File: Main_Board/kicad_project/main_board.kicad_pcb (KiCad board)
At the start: 4 copper layers, 235 parts, among them J1 MOTOR, J10 USB_B_Micro, J11 DATA_UART, J12 I2C_EXTERNAL, J13 DEBUG_HEADER, J14 IO1, J15 IO7, J16 IO2, J17 IO3, J18 IO8, J19 IO9, J2 MOTOR, J20 IO4, J21 IO5, J22 IO10, J23 IO6, J24 EXPANSION_HEADER, J3 MOTOR, J4 MOTOR, J5 PWR_ENTRY, J6 12V_HDR, J7 3V3_HDR, J8 5V_HDR, J9 I2C_BUFFERED, SW1 SW_SPST, U1 TMC2209, U2 TMC2209, U3 TMC2209, U4 TMC2209, U5 TPS562200, U6 TPS562200, U7 PCA9600DP, U8 USBLC6-2SC6, U9 STM32G474VxT, Y1 ABS06-32.768kHz, Y2 DNP

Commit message: edits to stepper layout
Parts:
- moved TP2 116.9 mm to (102.3, 53.3)
- moved TP3 116.9 mm to (130.8, 53.3)
- moved TP4 115.7 mm to (158.9, 53.3)
- moved TP1 115.6 mm to (74.3, 53.3)
- moved C11 113.0 mm to (100.7, 42.4)
- moved C13 113.0 mm to (103.1, 43.9)
- moved C17 113.0 mm to (98.2, 34.9)
- moved C18 113.0 mm to (92.0, 32.9)
- moved C2 113.0 mm to (72.7, 42.4)
- moved C20 113.0 mm to (129.1, 42.4)
- moved C25 113.0 mm to (142.0, 34.9)
- moved C26 113.0 mm to (126.4, 34.9)
- moved C28 113.0 mm to (167.0, 41.6)
- moved C29 113.0 mm to (157.3, 42.4)
- moved C31 113.0 mm to (159.7, 43.9)
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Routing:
- added copper zone on In2.Cu, net +12V
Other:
- board outline added: 150 x 150 mm

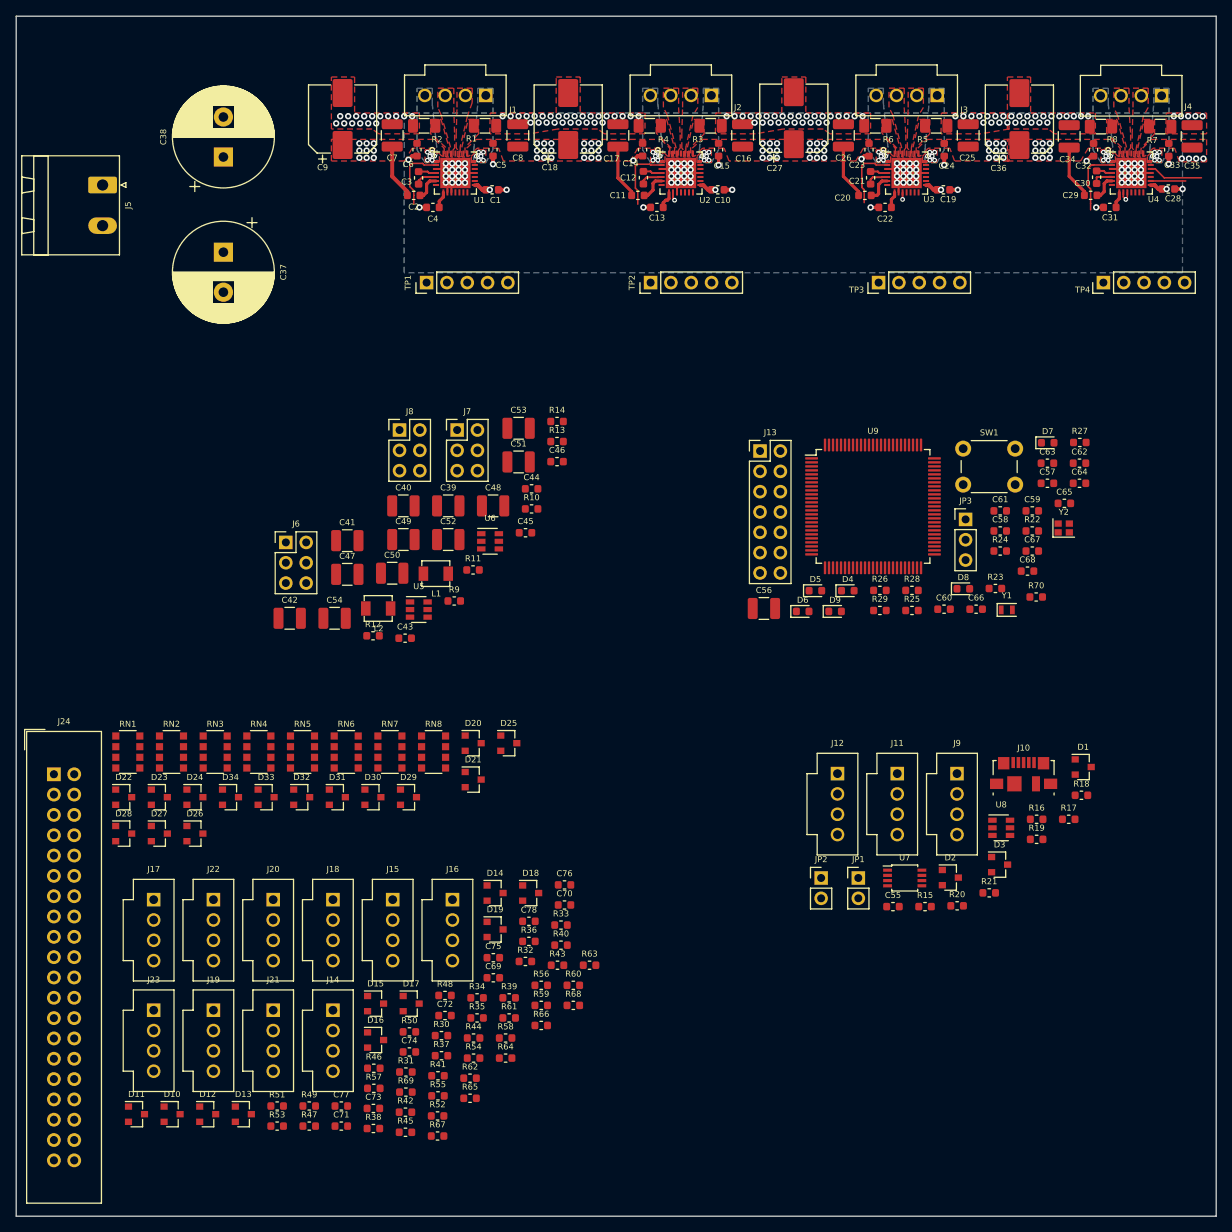
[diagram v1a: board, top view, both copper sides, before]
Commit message: regulators layout done
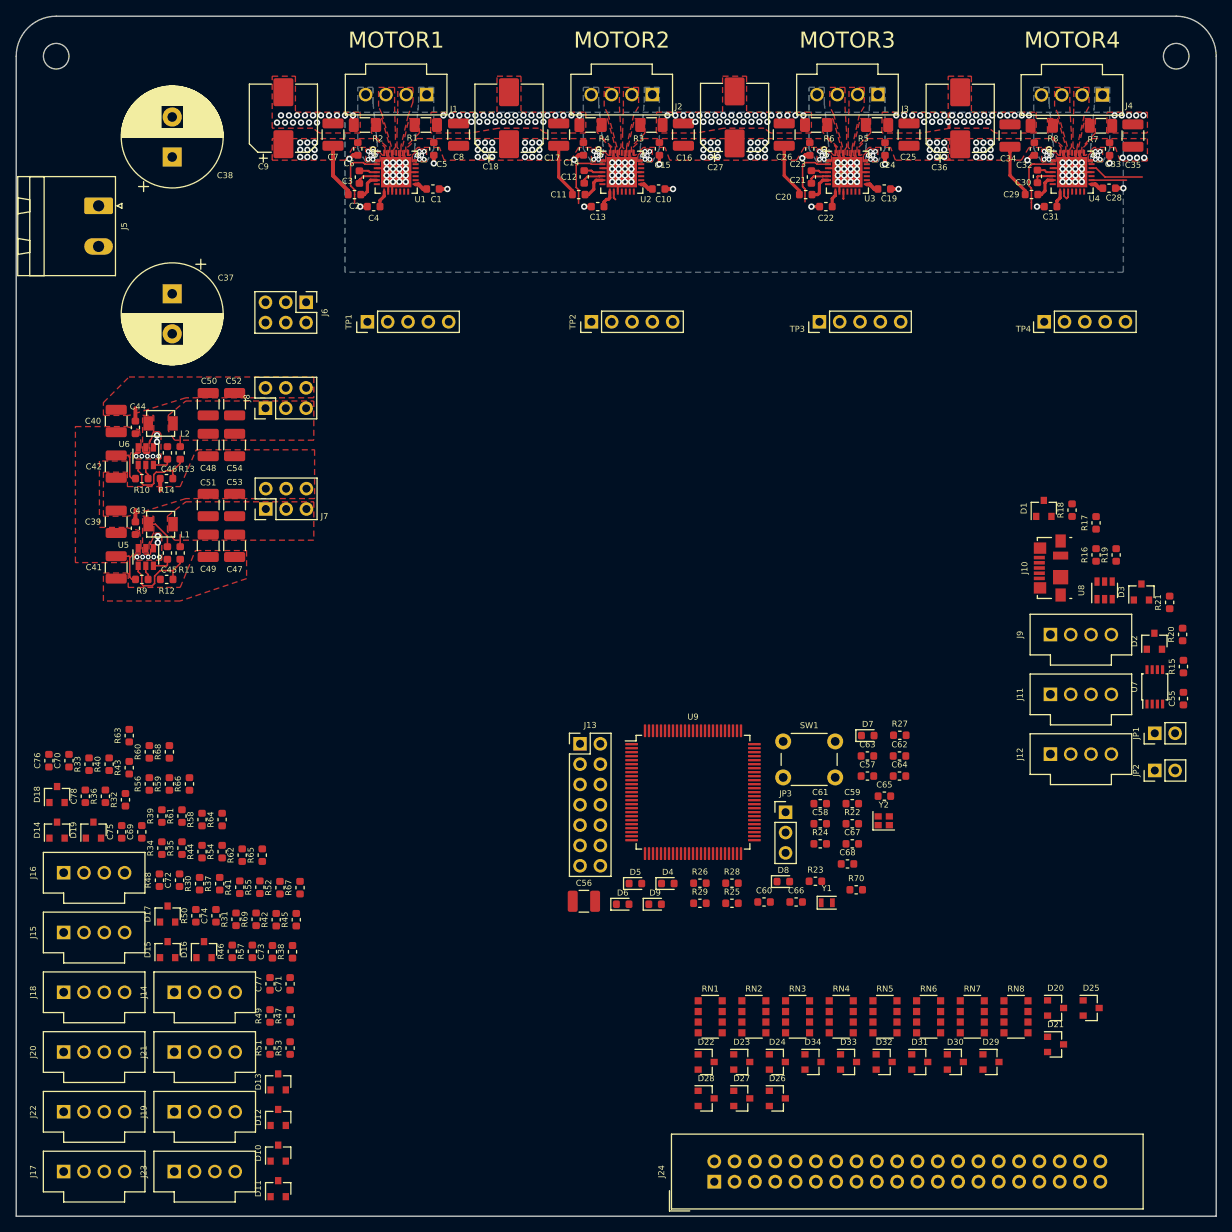
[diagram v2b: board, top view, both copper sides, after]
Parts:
- added REF**: MountingHole_3.2mm_M3, MountingHole:MountingHole_3.2mm_M3, F.Cu at (28.0, 25.0)
- added REF**: MountingHole_3.2mm_M3, MountingHole:MountingHole_3.2mm_M3, F.Cu at (168.0, 25.0)
- moved J24 97.0 mm to (110.3, 165.7), turned to 90 degrees
- moved RN1 80.0 mm to (109.8, 145.1)
- moved RN3 80.0 mm to (120.7, 145.1)
- moved RN5 80.0 mm to (131.6, 145.1)
- moved D23 80.0 mm to (113.7, 150.7)
- moved D24 80.0 mm to (118.1, 150.7)
- moved D25 80.0 mm to (157.4, 144.0)
- moved D26 80.0 mm to (118.1, 155.3)
- moved D27 80.0 mm to (113.7, 155.3)
- moved D29 80.0 mm to (144.8, 150.7)
- moved D31 80.0 mm to (135.9, 150.7)
- moved D32 80.0 mm to (131.5, 150.7)
- moved RN2 80.0 mm to (115.2, 145.1)
- moved RN4 80.0 mm to (126.1, 145.1)
- moved RN7 80.0 mm to (142.5, 145.1)
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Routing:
- net Net-(R13-Pad2): track 0.00 -> 11.5 mm
- net Net-(R11-Pad2): track 0.00 -> 10.7 mm
- net +12V: track 27.3 -> 37.5 mm
- net GND: track 45.7 -> 50.3 mm, vias 184 -> 198
- net Net-(C45-Pad1): track 0.00 -> 3.73 mm
- net Net-(C46-Pad2): track 0.00 -> 2.85 mm
- net Net-(C45-Pad2): track 0.00 -> 2.50 mm
- net Net-(R9-Pad1): track 0.00 -> 1.82 mm
- net Net-(R10-Pad1): track 0.00 -> 1.82 mm
- net +5V: track 0.00 -> 1.30 mm
- net +3V3: track 12.4 -> 11.9 mm, vias 7 -> 0
- added copper zone on F.Cu, net +3V3
- added copper zone on F.Cu, net +5V
- added copper zone on F.Cu, net Net-(C45-Pad1)
- added copper zone on F.Cu, net Net-(C46-Pad1)
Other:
- outline, holes or cut-outs redrawn
- board text added: "MOTOR1"
- board text added: "MOTOR2"
- board text added: "MOTOR3"
- board text added: "MOTOR4"

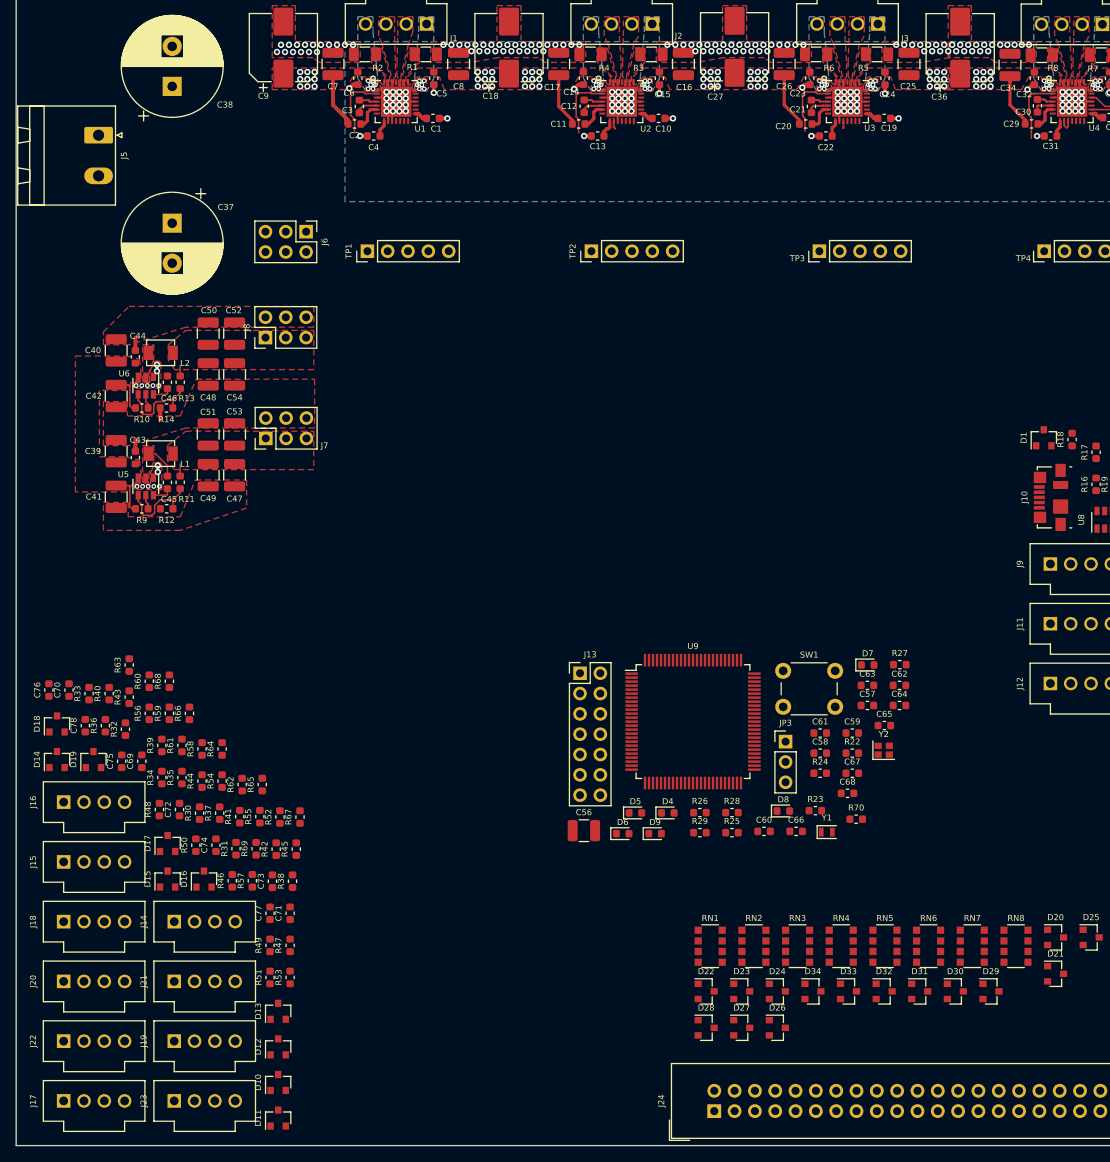
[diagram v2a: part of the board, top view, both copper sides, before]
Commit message: limit switch layout
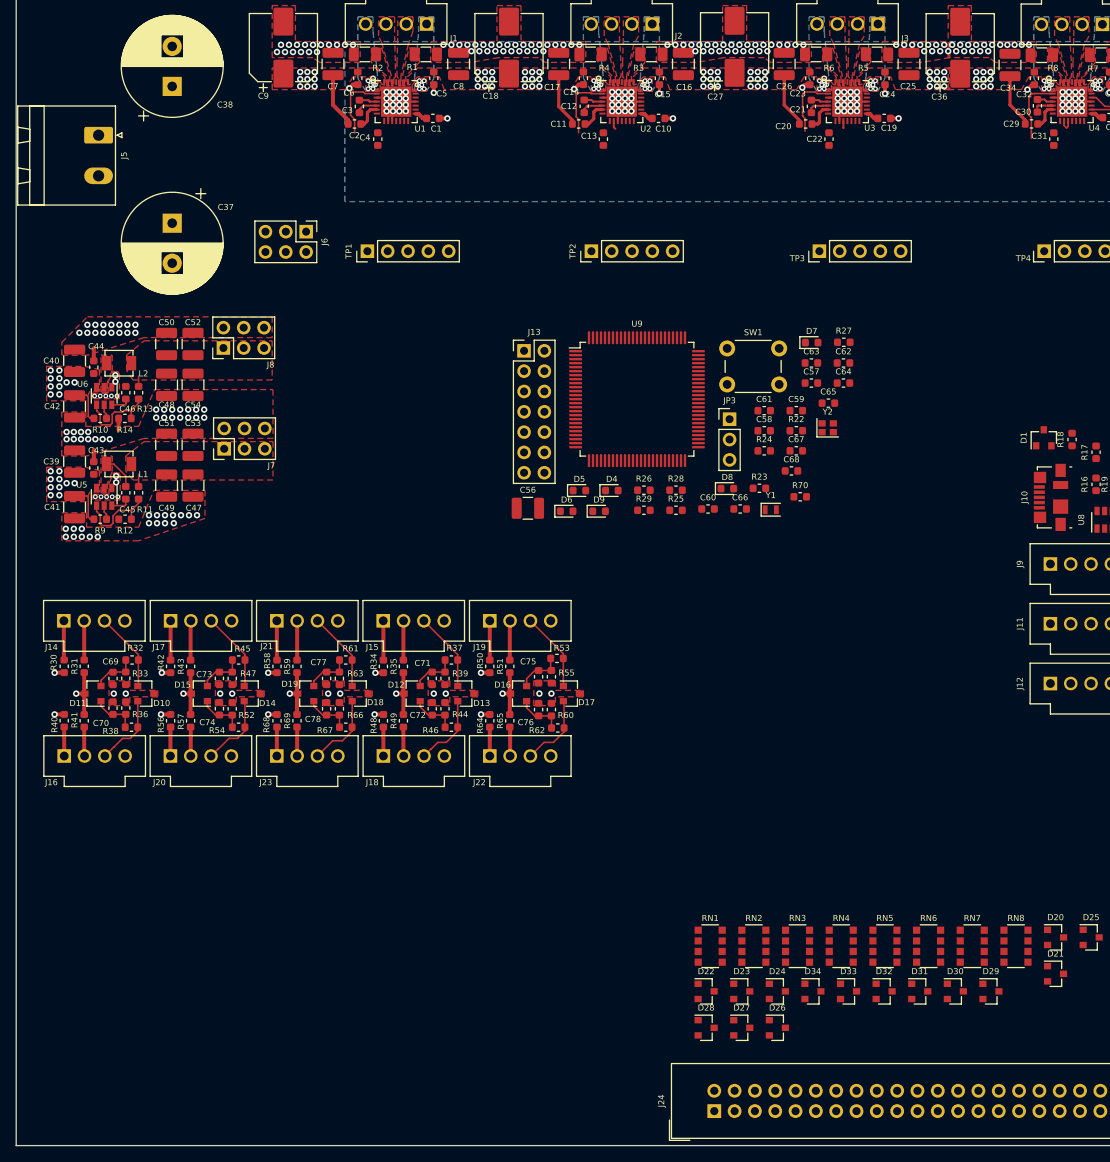
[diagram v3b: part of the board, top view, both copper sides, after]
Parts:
- moved J19 65.7 mm to (82.2, 104.4)
- moved J22 64.1 mm to (82.2, 121.3)
- moved J17 61.5 mm to (42.3, 104.4)
- moved C76 61.3 mm to (88.3, 115.5), turned to 270 degrees
- moved D11 57.9 mm to (32.6, 113.5), turned to 180 degrees
- moved D17 53.8 mm to (92.4, 113.5), turned to 0 degrees
- moved C75 53.2 mm to (88.3, 111.4), turned to 270 degrees
- moved R53 52.0 mm to (90.6, 109.1), turned to 0 degrees
- moved D10 51.3 mm to (39.2, 113.5), turned to 0 degrees
- moved R60 50.4 mm to (89.9, 115.5), turned to 270 degrees
- moved J15 50.0 mm to (68.9, 104.4)
- moved R51 49.1 mm to (84.7, 110.1)
- moved D12 47.2 mm to (72.5, 113.5), turned to 180 degrees
- moved J21 46.9 mm to (55.6, 104.4)
- moved D13 46.1 mm to (79.2, 113.5), turned to 0 degrees
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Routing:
- net +3V3: track 11.9 -> 43.5 mm, vias 0 -> 5
- net +12V: track 37.5 -> 48.7 mm, vias 67 -> 97
- net Net-(D18-Pad1): track 0.00 -> 9.95 mm
- net Net-(D14-Pad1): track 0.00 -> 9.94 mm
- net Net-(D10-Pad1): track 0.00 -> 9.94 mm
- net Net-(D13-Pad1): track 0.00 -> 9.91 mm
- net Net-(D17-Pad1): track 0.00 -> 9.86 mm
- net Net-(D18-Pad2): track 0.00 -> 9.35 mm
- net Net-(D17-Pad2): track 0.00 -> 9.32 mm
- net Net-(D14-Pad2): track 0.00 -> 9.28 mm
- net Net-(D13-Pad2): track 0.00 -> 9.23 mm
- net Net-(D10-Pad2): track 0.00 -> 9.14 mm
- net /Limit Switches/IO9: track 0.00 -> 5.99 mm
- net /Limit Switches/IO10: track 0.00 -> 5.85 mm
- net /Limit Switches/IO2: track 0.00 -> 5.80 mm
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
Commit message: expansion connector - rev 1.1 schematic, finished layout
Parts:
- moved D27 40.4 mm to (153.8, 151.2), turned to 90 degrees
- moved D20 40.3 mm to (113.3, 151.1), turned to 90 degrees
- moved D23 37.2 mm to (150.8, 147.7), turned to 90 degrees
- moved D22 30.1 mm to (139.2, 147.7), turned to 90 degrees
- moved D25 30.0 mm to (127.5, 147.6), turned to 90 degrees
- moved D21 28.2 mm to (124.8, 151.1), turned to 90 degrees
- moved D34 25.5 mm to (148.1, 151.2), turned to 90 degrees
- moved D26 24.5 mm to (142.2, 151.2), turned to 90 degrees
- moved D31 20.8 mm to (156.6, 147.7), turned to 90 degrees
- moved D29 14.2 mm to (130.7, 151.1), turned to 90 degrees
- moved J10 14.1 mm to (163.0, 79.8)
- moved RN8 13.8 mm to (155.5, 156.6), turned to 270 degrees
- moved RN7 13.6 mm to (149.7, 156.6), turned to 270 degrees
- moved RN6 13.4 mm to (143.9, 156.6), turned to 270 degrees
- moved RN5 13.2 mm to (138.1, 156.6), turned to 270 degrees
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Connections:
- D22 pad 1: /MCU/EXP_IO16 -> /MCU/EXP_IO17
- D22 pad 2: /MCU/EXP_IO17 -> /MCU/EXP_IO18
- D23 pad 1: /MCU/EXP_IO24 -> /MCU/EXP_IO25
- D23 pad 2: /MCU/EXP_IO25 -> /MCU/EXP_IO26
- D26 pad 1: /MCU/EXP_IO18 -> /MCU/EXP_IO19
- D26 pad 2: /MCU/EXP_IO19 -> /MCU/EXP_IO20
- D27 pad 1: /MCU/EXP_IO26 -> /MCU/EXP_IO27
- D27 pad 2: /MCU/EXP_IO27 -> /MCU/EXP_IO28
- D30 pad 1: /MCU/EXP_IO20 -> /MCU/EXP_IO21
- D30 pad 2: /MCU/EXP_IO21 -> /MCU/EXP_IO22
- D31 pad 1: /MCU/EXP_IO28 -> /MCU/EXP_IO29
- D31 pad 2: /MCU/EXP_IO29 -> /MCU/EXP_IO30
- D33 pad 2: /MCU/EXP_IO30 -> /MCU/EXP_IO16
- D34 pad 1: /MCU/EXP_IO22 -> /MCU/EXP_IO23
- D34 pad 2: /MCU/EXP_IO23 -> /MCU/EXP_IO24
- RN1 pad 1: /MCU/EXP_IO1 -> /MCU/EXP_IO4
- RN1 pad 2: /MCU/EXP_IO2 -> /MCU/EXP_IO3
- RN1 pad 3: /MCU/EXP_IO3 -> /MCU/EXP_IO2
- RN1 pad 4: /MCU/EXP_IO4 -> /MCU/EXP_IO1
- RN1 pad 5: Net-(J24-Pad11) -> Net-(J24-Pad5)
- RN1 pad 6: Net-(J24-Pad9) -> Net-(J24-Pad6)
- RN1 pad 8: Net-(J24-Pad5) -> Net-(J24-Pad8)
- RN2 pad 1: /MCU/EXP_IO5 -> /MCU/EXP_IO8
- RN2 pad 2: /MCU/EXP_IO6 -> /MCU/EXP_IO7
- RN2 pad 3: /MCU/EXP_IO7 -> /MCU/EXP_IO6
- RN2 pad 4: /MCU/EXP_IO8 -> /MCU/EXP_IO5
- RN2 pad 5: Net-(J24-Pad21) -> Net-(J24-Pad9)
- RN2 pad 6: Net-(J24-Pad19) -> Net-(J24-Pad10)
- RN2 pad 7: Net-(J24-Pad17) -> Net-(J24-Pad11)
- RN2 pad 8: Net-(J24-Pad13) -> Net-(J24-Pad12)
- RN3 pad 1: /MCU/EXP_IO9 -> /MCU/EXP_IO12
- RN3 pad 2: /MCU/EXP_IO10 -> /MCU/EXP_IO11
- RN3 pad 3: /MCU/EXP_IO11 -> /MCU/EXP_IO10
- RN3 pad 4: /MCU/EXP_IO12 -> /MCU/EXP_IO9
- RN3 pad 5: Net-(J24-Pad31) -> Net-(J24-Pad13)
- RN3 pad 6: Net-(J24-Pad29) -> Net-(J24-Pad14)
- RN3 pad 7: Net-(J24-Pad25) -> Net-(J24-Pad17)
- RN3 pad 8: Net-(J24-Pad23) -> Net-(J24-Pad18)
- RN4 pad 1: /MCU/EXP_IO13 -> Net-(RN4-Pad1)
- RN4 pad 2: /MCU/EXP_IO14 -> Net-(RN4-Pad2)
- RN4 pad 3: /MCU/EXP_IO15 -> /MCU/EXP_IO14
- RN4 pad 4: Net-(RN4-Pad4) -> /MCU/EXP_IO13
- RN4 pad 5: Net-(RN4-Pad5) -> Net-(J24-Pad19)
- RN4 pad 6: Net-(J24-Pad37) -> Net-(J24-Pad20)
- RN4 pad 7: Net-(J24-Pad35) -> Net-(RN4-Pad7)
- RN4 pad 8: Net-(J24-Pad33) -> Net-(RN4-Pad8)
- RN5 pad 1: /MCU/EXP_IO16 -> /MCU/EXP_IO18
- RN5 pad 3: /MCU/EXP_IO18 -> /MCU/EXP_IO16
- RN5 pad 4: /MCU/EXP_IO19 -> /MCU/EXP_IO15
- RN5 pad 5: Net-(J24-Pad12) -> Net-(J24-Pad21)
- RN5 pad 6: Net-(J24-Pad10) -> Net-(J24-Pad22)
- RN5 pad 7: Net-(J24-Pad8) -> Net-(J24-Pad23)
- RN5 pad 8: Net-(J24-Pad6) -> Net-(J24-Pad24)
- RN6 pad 1: /MCU/EXP_IO20 -> /MCU/EXP_IO22
- RN6 pad 3: /MCU/EXP_IO22 -> /MCU/EXP_IO20
- RN6 pad 4: /MCU/EXP_IO23 -> /MCU/EXP_IO19
- RN6 pad 5: Net-(J24-Pad22) -> Net-(J24-Pad25)
- RN6 pad 6: Net-(J24-Pad20) -> Net-(J24-Pad26)
- RN6 pad 7: Net-(J24-Pad18) -> Net-(J24-Pad29)
- RN6 pad 8: Net-(J24-Pad14) -> Net-(J24-Pad30)
- RN7 pad 1: /MCU/EXP_IO24 -> /MCU/EXP_IO26
- RN7 pad 3: /MCU/EXP_IO26 -> /MCU/EXP_IO24
- RN7 pad 4: /MCU/EXP_IO27 -> /MCU/EXP_IO23
- RN7 pad 5: Net-(J24-Pad32) -> Net-(J24-Pad31)
- RN7 pad 6: Net-(J24-Pad30) -> Net-(J24-Pad32)
- RN7 pad 7: Net-(J24-Pad26) -> Net-(J24-Pad33)
- RN7 pad 8: Net-(J24-Pad24) -> Net-(J24-Pad34)
- RN8 pad 1: /MCU/EXP_IO28 -> /MCU/EXP_IO30
- RN8 pad 3: /MCU/EXP_IO30 -> /MCU/EXP_IO28
- RN8 pad 4: Net-(RN8-Pad4) -> /MCU/EXP_IO27
- RN8 pad 5: Net-(RN8-Pad5) -> Net-(J24-Pad35)
- RN8 pad 6: Net-(J24-Pad38) -> Net-(J24-Pad36)
- RN8 pad 7: Net-(J24-Pad36) -> Net-(J24-Pad37)
- RN8 pad 8: Net-(J24-Pad34) -> Net-(J24-Pad38)
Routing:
- net Net-(J24-Pad25): track 0.00 -> 9.10 mm
- net Net-(J24-Pad17): track 0.00 -> 9.01 mm
- net Net-(J24-Pad23): track 0.00 -> 8.90 mm
- net Net-(J24-Pad21): track 0.00 -> 8.81 mm
- net Net-(J24-Pad19): track 0.00 -> 8.76 mm
- net Net-(J24-Pad37): track 0.00 -> 8.72 mm
- net Net-(J24-Pad35): track 0.00 -> 8.64 mm
- net Net-(J24-Pad5): track 0.00 -> 8.60 mm
- net Net-(J24-Pad7): track 0.00 -> 8.55 mm
- net Net-(J24-Pad33): track 0.00 -> 8.44 mm
- net Net-(J24-Pad31): track 0.00 -> 8.36 mm
- net Net-(J24-Pad9): track 0.00 -> 8.30 mm
- net Net-(J24-Pad11): track 0.00 -> 8.25 mm
- net Net-(J24-Pad13): track 0.00 -> 8.25 mm
- net Net-(J24-Pad29): track 0.00 -> 8.11 mm
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- added copper zone on In2.Cu, net +3V3
